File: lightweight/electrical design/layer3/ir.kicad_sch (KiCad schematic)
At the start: 41 parts, among them J1 SH1.0 Female, SW3 SW_Push, U1 STM32F103C8T6, Y1 Crystal

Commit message: update lw pcbs
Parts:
- added SW2: SW_DPDT_x2, Switches:SWITCH_SPDT_PTH_11.6X4.0MM_LOCK, symbol Switch:SW_DPDT_x2
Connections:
- net +3V3: now also SW2.1 (A); no longer C4.2, C5.2, C6.2, FB1.1, R41.2, U1.24 (VDD), U1.36 (VDD), U1.48 (VDD)
- net IR18: now also U1.45 (PB8); no longer U1.34 (PA13)
- net IR19: now also U1.43 (PB7); no longer U1.37 (PA14)
- net SWDCLOCK: now also U1.37 (PA14)
- net SWDIO: now also U1.34 (PA13)
- new net MCU3V3: C4.2, C5.2, C6.2, FB1.1, R41.2, SW2.2 (B), U1.24 (VDD), U1.36 (VDD), U1.48 (VDD)

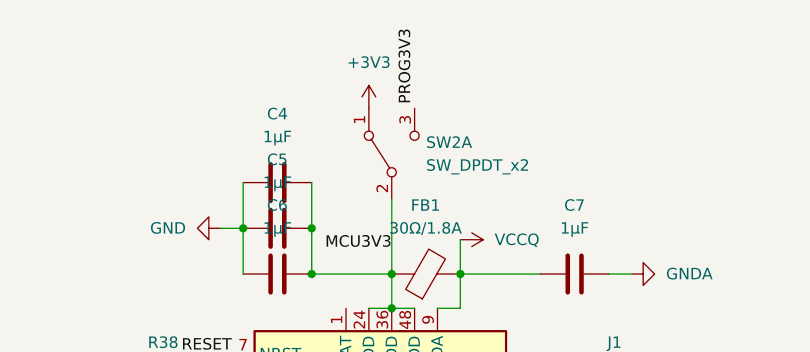
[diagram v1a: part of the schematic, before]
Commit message: move stuff around layer 3; add stm32 prog switch
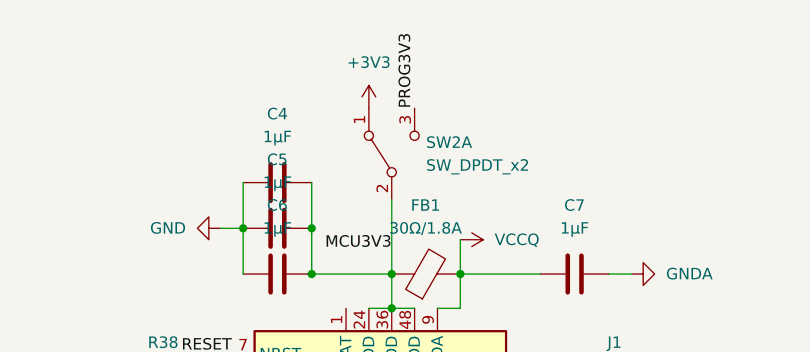
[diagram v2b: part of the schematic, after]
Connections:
- net PROG3V3: now also SW2.3 (C)
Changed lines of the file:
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@@
     (effects (font (size 1.27 1.27)) (justify left bottom))
   )
-  (label "PROG3V3" (at 208.28 18.415 270) (fields_autoplaced)
-    (effects (font (size 1.27 1.27)) (justify right bottom))
+  (label "PROG3V3" (at 208.28 27.305 90) (fields_autoplaced)
+    (effects (font (size 1.27 1.27)) (justify left bottom))
   )
   (label "IR1" (at 187.96 72.39 180) (fields_autoplaced)

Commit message: update lw l3 pcb
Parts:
- removed FB1, FB2: 30Ω/1.8A, Capacitor_SMD:C_0603_1608Metric, symbol Device:FerriteBead
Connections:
- net GND: now also C7.1, U1.8 (VSSA)
- net IR1: now also U1.12 (PA2); no longer U1.2 (PC13)
- net IR10: now also U1.42 (PB6); no longer U1.17 (PA7)
- net IR11: now also U1.41 (PB5); no longer U1.18 (PB0)
- net IR12: now also U1.40 (PB4); no longer U1.20 (PB2)
- net IR13: now also U1.39 (PB3); no longer U1.25 (PB12)
- net IR14: now also U1.38 (PA15); no longer U1.26 (PB13)
- net IR15: now also U1.33 (PA12); no longer U1.27 (PB14)
- net IR16: now also U1.32 (PA11); no longer U1.28 (PB15)
- net IR17: no longer U1.33 (PA12)
- net IR18: now also U1.28 (PB15); no longer U1.45 (PB8)
- net IR19: now also U1.27 (PB14); no longer U1.43 (PB7)
- net IR2: now also U1.11 (PA1); no longer U1.3 (PC14)
- net IR20: now also U1.18 (PB0); no longer U1.38 (PA15)
- net IR21: now also U1.17 (PA7); no longer U1.39 (PB3)
- net IR22: now also U1.16 (PA6); no longer U1.40 (PB4)
- net IR23: now also U1.15 (PA5); no longer U1.41 (PB5)
- net IR24: now also U1.14 (PA4); no longer U1.42 (PB6)
- net IR3: now also U1.10 (PA0); no longer U1.4 (PC15)
- net IR4: now also U1.4 (PC15); no longer U1.10 (PA0)
- net IR5: now also U1.3 (PC14); no longer U1.11 (PA1)
- net IR6: now also U1.2 (PC13); no longer U1.12 (PA2)
- net IR7: now also U1.46 (PB9); no longer U1.14 (PA4)
- net IR8: now also U1.45 (PB8); no longer U1.15 (PA5)
- net IR9: now also U1.43 (PB7); no longer U1.16 (PA6)
- net MCU3V3: now also C7.2, U1.9 (VDDA)
- removed net GNDA: C7.2, U1.8 (VSSA)
- removed net VCCQ: C7.1, U1.9 (VDDA)

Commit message: rerouted lw l3 ir stm circuit
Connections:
- net IR1: now also U1.17 (PA7); no longer U1.12 (PA2)
- net IR17: now also U1.29 (PA8)
- net IR2: now also U1.16 (PA6); no longer U1.11 (PA1)
- net IR20: now also U1.26 (PB13); no longer U1.18 (PB0)
- net IR21: now also U1.25 (PB12); no longer U1.17 (PA7)
- net IR22: now also U1.20 (PB2); no longer U1.16 (PA6)
- net IR23: now also U1.19 (PB1); no longer U1.15 (PA5)
- net IR24: now also U1.18 (PB0); no longer U1.14 (PA4)
- net IR3: now also U1.15 (PA5); no longer U1.10 (PA0)
- net IR4: now also U1.12 (PA2); no longer U1.4 (PC15)
- net IR5: now also U1.11 (PA1); no longer U1.3 (PC14)
- net IR6: now also U1.10 (PA0); no longer U1.2 (PC13)
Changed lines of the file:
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@@
     (stroke (width 0) (type default))
+  )
+  (label "IR5" (at 220.98 85.09 0) (fields_autoplaced)
+    (effects (font (size 1.27 1.27)) (justify left bottom))
+  )
+  (label "IR22" (at 187.96 87.63 180) (fields_autoplaced)
+    (effects (font (size 1.27 1.27)) (justify right bottom))
   )
   (label "IR20" (at 135.89 108.712 0) (fields_autoplaced)
@@
     (effects (font (size 1.27 1.27)) (justify right bottom))
   )
-  (label "IR1" (at 220.98 87.63 0) (fields_autoplaced)
+  (label "IR6" (at 220.98 82.55 0) (fields_autoplaced)
     (effects (font (size 1.27 1.27)) (justify left bottom))
   )
@@
     (effects (font (size 1.27 1.27)) (justify left bottom))
   )
-  (label "IR4" (at 187.96 77.47 180) (fields_autoplaced)
-    (effects (font (size 1.27 1.27)) (justify right bottom))
+  (label "IR18" (at 73.66 108.712 0) (fields_autoplaced)
+    (effects (font (size 1.27 1.27)) (justify left bottom))
   )
-  (label "IR18" (at 73.66 108.712 0) (fields_autoplaced)
+  (label "IR4" (at 220.98 87.63 0) (fields_autoplaced)
     (effects (font (size 1.27 1.27)) (justify left bottom))
   )
   (label "OSCOUT" (at 187.96 67.31 180) (fields_autoplaced)
     (effects (font (size 1.27 1.27)) (justify right bottom))
-  )
-  (label "IR24" (at 220.98 92.71 0) (fields_autoplaced)
-    (effects (font (size 1.27 1.27)) (justify left bottom))
   )
   (label "DEBUGRX" (at 234.95 58.42 0) (fields_autoplaced)
@@
     (effects (font (size 1.27 1.27)) (justify left bottom))
   )
-  (label "IR20" (at 187.96 82.55 180) (fields_autoplaced)
+  (label "IR20" (at 187.96 115.57 180) (fields_autoplaced)
     (effects (font (size 1.27 1.27)) (justify right bottom))
   )
@@
     (effects (font (size 1.27 1.27)) (justify left bottom))
   )
-  (label "DEBUGTX" (at 234.95 60.96 0) (fields_autoplaced)
+  (label "IR23" (at 187.96 85.09 180) (fields_autoplaced)
+    (effects (font (size 1.27 1.27)) (justify right bottom))
+  )
+  (label "IR21" (at 187.96 113.03 180) (fields_autoplaced)
+    (effects (font (size 1.27 1.27)) (justify right bottom))
+  )
+  (label "IR2" (at 220.98 97.79 0) (fields_autoplaced)
     (effects (font (size 1.27 1.27)) (justify left bottom))
   )
-  (label "IR2" (at 220.98 85.09 0) (fields_autoplaced)
+  (label "DEBUGTX" (at 234.95 60.96 0) (fields_autoplaced)
     (effects (font (size 1.27 1.27)) (justify left bottom))
   )
@@
   )
   (label "IR19" (at 187.96 118.11 180) (fields_autoplaced)
-    (effects (font (size 1.27 1.27)) (justify right bottom))
-  )
-  (label "IR5" (at 187.96 74.93 180) (fields_autoplaced)
-    (effects (font (size 1.27 1.27)) (justify right bottom))
-  )
-  (label "IR6" (at 187.96 72.39 180) (fields_autoplaced)
     (effects (font (size 1.27 1.27)) (justify right bottom))
   )
@@
     (effects (font (size 1.27 1.27)) (justify left bottom))
   )
+  (label "IR1" (at 220.98 100.33 0) (fields_autoplaced)
+    (effects (font (size 1.27 1.27)) (justify left bottom))
+  )
   (label "OSCIN" (at 260.35 115.57 90) (fields_autoplaced)
     (effects (font (size 1.27 1.27)) (justify left bottom))
+  )
+  (label "IR24" (at 187.96 82.55 180) (fields_autoplaced)
+    (effects (font (size 1.27 1.27)) (justify right bottom))
   )
   (label "SWDCLOCK" (at 234.95 68.58 0) (fields_autoplaced)
@@
     (effects (font (size 1.27 1.27)) (justify left bottom))
   )
-  (label "IR22" (at 220.98 97.79 0) (fields_autoplaced)
-    (effects (font (size 1.27 1.27)) (justify left bottom))
-  )
-  (label "IR23" (at 220.98 95.25 0) (fields_autoplaced)
+  (label "IR3" (at 220.98 95.25 0) (fields_autoplaced)
     (effects (font (size 1.27 1.27)) (justify left bottom))
   )
@@
   (label "IR7" (at 187.96 105.41 180) (fields_autoplaced)
     (effects (font (size 1.27 1.27)) (justify right bottom))
-  )
-  (label "IR3" (at 220.98 82.55 0) (fields_autoplaced)
-    (effects (font (size 1.27 1.27)) (justify left bottom))
   )
   (label "SWDCLOCK" (at 220.98 118.11 0) (fields_autoplaced)
@@
     (effects (font (size 1.27 1.27)) (justify left bottom))
   )
-  (label "IR21" (at 220.98 100.33 0) (fields_autoplaced)
+  (label "IR17" (at 220.98 102.87 0) (fields_autoplaced)
     (effects (font (size 1.27 1.27)) (justify left bottom))
   )
